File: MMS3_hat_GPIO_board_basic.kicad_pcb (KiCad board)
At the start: 4 copper layers, 100 x 50 mm, 55 parts, among them J1 Chainbus in, J2 Chainbus Out, J3 Conn_01x04_Pin, J4 AMASS XT60 Male, J5 AMASS XT60 Female, J8 Conn_01x03_Pin, SW1 SW_DIP_x04, U1 SN74CB3Q3384APW, U2 M24C64, U4 AMS1117, U5 LM2596HVS-ADJRG

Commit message: added routing and gerber
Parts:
- removed C16, C18: 10uF, PCM_JLCPCB:C_0603
- removed C17, C19, C25, C26, C27, C28: 47u, Capacitor_SMD:CP_Elec_6.3x7.7
- removed C20, C21, C23, C24: 100nF, PCM_JLCPCB:C_0603
- removed C22: 3.3nF, PCM_JLCPCB:C_0603
- removed D2, D4: MBRD10100CTTR, SMC_MBRD10100CTTR:TO-252-3_L6.5-W5.8-P4.58-TL
- removed J4: AMASS XT60 Male, XT60:AMASS_XT60PW-M_1x02_P7.20mm_Horizontal
- removed L1: 100uH 4A, Inductor_SMD:L_Sunlord_SWRB1207S
- removed R10, R11, R17, R18: 33kΩ, PCM_JLCPCB:R_0402
- removed R12: 1kΩ, PCM_JLCPCB:R_0402
- removed R13: 18.7k, PCM_JLCPCB:R_0402
- removed R14: 16.5k, PCM_JLCPCB:R_0402
- removed R15: 9.53k, PCM_JLCPCB:R_0402
- removed R16: 5.11k, PCM_JLCPCB:R_0402
- removed SW1: SW_DIP_x04, Button_Switch_THT:SW_DIP_SPSTx04_Slide_6.7x11.72mm_W7.62mm_P2.54mm_LowProfile
- removed TP8: TestPoint, TestPoint:TestPoint_Pad_D1.0mm
- removed U5: LM2596HVS-ADJRG, Package_TO_SOT_SMD:TO-263-5_TabPin3
- added C3: 10uF, PCM_JLCPCB:C_0603, F.Cu at (107.8, 106.0)
- added C4: 10uF, PCM_JLCPCB:C_0603, F.Cu at (110.3, 110.9)
- added C5: 10uF, PCM_JLCPCB:C_0603, F.Cu at (108.6, 110.9)
- added C6: 100n, PCM_JLCPCB:C_0603, F.Cu at (131.0, 111.5)
- added J10: Conn_01x03_Pin, Connector_JST:JST_XH_S3B-XH-A_1x03_P2.50mm_Horizontal, F.Cu at (125.7, 133.6)
- added J11: Conn_01x03_Pin, Connector_JST:JST_XH_S3B-XH-A_1x03_P2.50mm_Horizontal, F.Cu at (137.7, 133.6)
- added J12: Conn_01x03_Pin, Connector_JST:JST_XH_S3B-XH-A_1x03_P2.50mm_Horizontal, F.Cu at (149.6, 133.6)
- added J13: Conn_01x03_Pin, Connector_JST:JST_XH_S3B-XH-A_1x03_P2.50mm_Horizontal, F.Cu at (161.6, 133.6)
- added J14: Conn_01x03_Pin, Connector_JST:JST_XH_S3B-XH-A_1x03_P2.50mm_Horizontal, F.Cu at (174.6, 127.4)
- added J15: Conn_01x03_Pin, Connector_JST:JST_XH_S3B-XH-A_1x03_P2.50mm_Horizontal, F.Cu at (174.6, 115.5)
- added J16: Conn_01x03_Pin, Connector_JST:JST_XH_S3B-XH-A_1x03_P2.50mm_Horizontal, F.Cu at (174.6, 103.5)
- added J6: Conn_01x03_Pin, Connector_JST:JST_XH_S3B-XH-A_1x03_P2.50mm_Horizontal, F.Cu at (82.4, 122.4)
- added J7: Conn_01x03_Pin, Connector_JST:JST_XH_S3B-XH-A_1x03_P2.50mm_Horizontal, F.Cu at (89.5, 133.6)
- added J9: Conn_01x03_Pin, Connector_JST:JST_XH_S3B-XH-A_1x03_P2.50mm_Horizontal, F.Cu at (113.8, 133.6)
- added PIN 1: Conn_01x03_Pin, Connector_JST:JST_XH_S3B-XH-A_1x03_P2.50mm_Horizontal, F.Cu at (82.4, 98.5)
- added U3: AMS1117, PCM_JLCPCB:SOT-223-3_L6.5-W3.4-P2.30-LS7.0-BR, F.Cu at (103.0, 110.0)
- J5: value AMASS XT60 Female -> Conn_01x03_Pin; footprint XT60:AMASS_XT60PW-F_1x02_P7.20mm_Horizontal -> Connector_JST:JST_XH_S3B-XH-A_1x03_P2.50mm_Horizontal
- J8: footprint Connector_PinHeader_2.54mm:PinHeader_1x03_P2.54mm_Vertical -> Connector_JST:JST_XH_S3B-XH-A_1x03_P2.50mm_Horizontal
- U4: value AMS1117 -> TCA9535PWR; footprint PCM_JLCPCB:SOT-223-3_L6.5-W3.4-P2.30-LS7.0-BR -> Package_SO:TSSOP-24_4.4x7.8mm_P0.65mm
- moved U4 41.4 mm to (127.7, 117.2)
- moved J8 10.9 mm to (101.5, 133.6), turned to 0 degrees
- moved J5 10.2 mm to (82.4, 110.5), turned to -90 degrees
- moved D1 9.75 mm to (168.0, 95.0)
- moved R1 9.75 mm to (166.2, 94.7)
- moved R2 0.94 mm to (157.5, 96.9)
- moved R3 0.89 mm to (158.6, 96.9)
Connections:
- J5 pad 2: Vin -> /GPIO_Expander/P01
- J8 pad 1: Net-(J8-Pin_1) -> GND
- J8 pad 2: Vin -> /GPIO_Expander/P04
- J8 pad 3: U_reg -> +3V3
- U4 pad 1: GND -> unconnected-(U4-~{INT}-Pad1)
- U4 pad 2: +3V3 -> GND
- U4 pad 3: +5V -> GND
- U4 pad 4: +3V3 -> /GPIO_Expander/P00
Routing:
- net +3V3: track 46.9 -> 291.5 mm, vias 1 -> 4
- net Vin: track 64.3 -> 0.00 mm
- net U_reg: track 55.0 -> 0.00 mm, vias 2 -> 0
- net /GPIO_Expander/P14: track 0.00 -> 51.4 mm
- net /GPIO_Expander/P00: track 0.00 -> 48.4 mm, vias 0 -> 1
- net /GPIO_Expander/P13: track 0.00 -> 46.4 mm
- net /GPIO_Expander/P12: track 0.00 -> 46.2 mm
- net /GPIO_Expander/P02: track 0.00 -> 45.7 mm
- net /GPIO_Expander/P01: track 0.00 -> 43.7 mm
- net /GPIO_Expander/P03: track 0.00 -> 39.4 mm
- net /GPIO_Expander/P11: track 0.00 -> 39.1 mm
- net Net-(U5-FB): track 38.3 -> 0.00 mm, vias 1 -> 0
- net +5V: track 59.4 -> 25.8 mm, vias 5 -> 3
- net /GPIO_Expander/P04: track 0.00 -> 27.2 mm
- net BRD_VIN: track 27.1 -> 0.00 mm
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- removed copper zone on In1.Cu, net GND
- removed copper zone on In2.Cu, net GND
- removed copper zone on F.Cu, net Net-(C20-Pad2)
- removed copper zone on F.Cu, net Net-(C23-Pad2)
- removed copper zone on F.Cu, net Net-(D4-K)
- removed copper zone on F.Cu, net Net-(J8-Pin_1)
- removed copper zone on F.Cu, net U_reg
- removed copper zone on B.Cu, net Vin
- removed copper zone on F.Cu, net Vin
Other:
- copper layers 4 -> 2
- board text added: "PIN 1"
- board text added: "PIN 10"
- board text added: "PIN 11"
- board text added: "PIN 12"
- board text added: "PIN 13"
- board text added: "PIN 2"
- board text added: "PIN 3"
- board text added: "PIN 4"
- board text added: "PIN 5"
- board text added: "PIN 6"
- board text added: "PIN 7"
- board text added: "PIN 8"
- board text added: "PIN 9"
- board text removed: "DONT change SW1 WITH POWER ON"
- board text removed: "SW1 24 9 12 6.2"

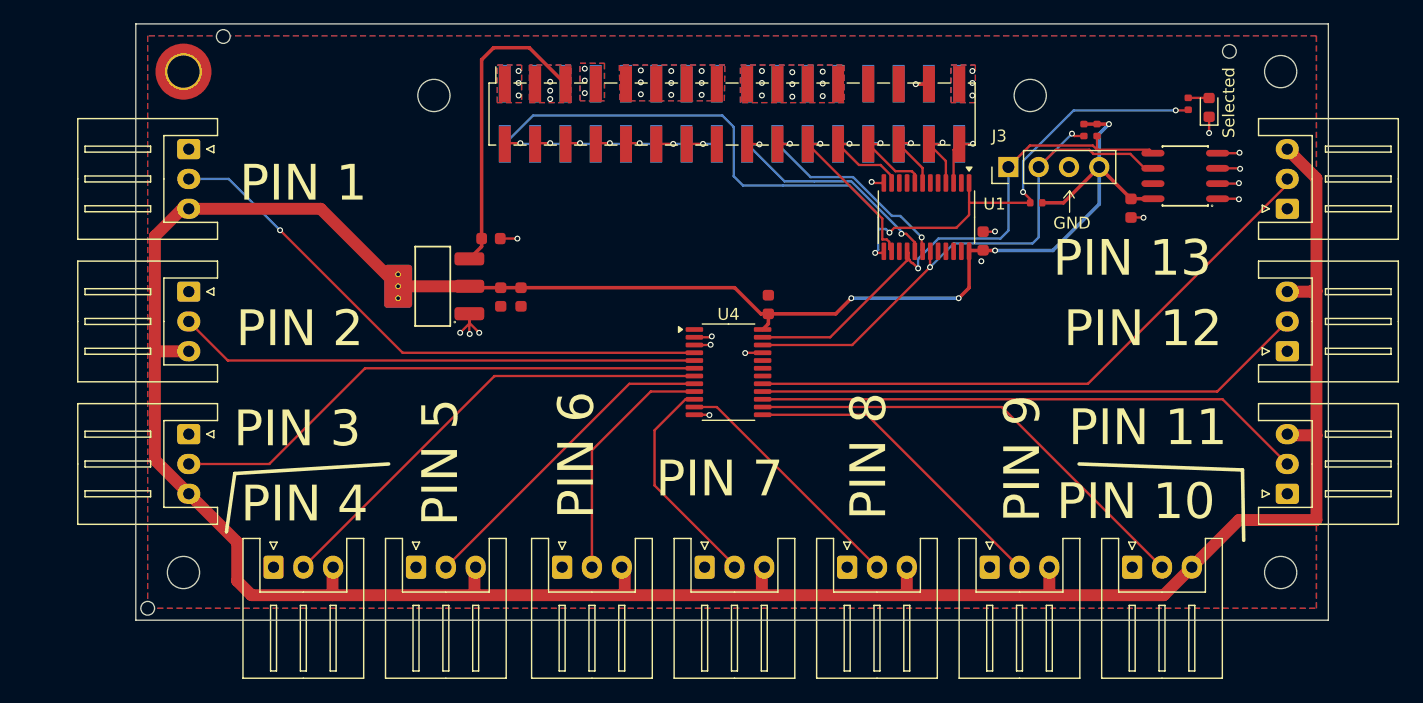
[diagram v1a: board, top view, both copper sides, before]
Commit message: added adc
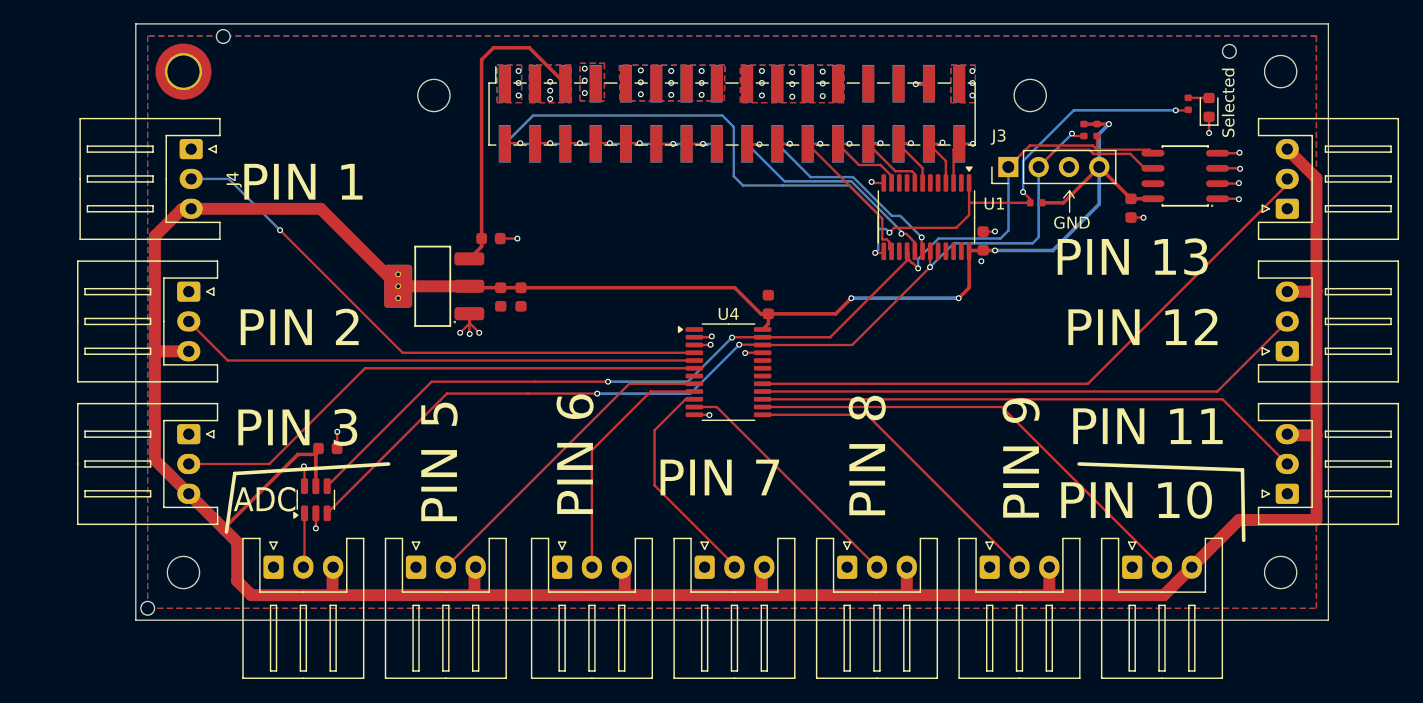
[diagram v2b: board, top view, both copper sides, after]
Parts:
- removed PIN 1: Conn_01x03_Pin, Connector_JST:JST_XH_S3B-XH-A_1x03_P2.50mm_Horizontal
- added C7: 100n, PCM_JLCPCB:C_0603, F.Cu at (94.1, 123.6)
- added J4: Conn_01x03_Pin, Connector_JST:JST_XH_S3B-XH-A_1x03_P2.50mm_Horizontal, F.Cu at (82.6, 98.5)
- added U5: MCP3421A0T-ECH, Package_TO_SOT_SMD:SOT-23-6, F.Cu at (93.1, 127.9)
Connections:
- J7 pad 2: /GPIO_Expander/P03 -> /GPIO_Expander/ADC
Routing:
- net /Bus_switch/Chainbus.SCL: track 50.0 -> 92.4 mm, vias 2 -> 4
- net /Bus_switch/Chainbus.SDA: track 46.4 -> 88.1 mm, vias 1 -> 3
- net /GPIO_Expander/P03: track 39.4 -> 0.00 mm
- net +3V3: track 291.5 -> 305.0 mm
- net /GPIO_Expander/ADC: track 0.00 -> 4.56 mm
- net GND: track 24.7 -> 29.1 mm, vias 35 -> 38
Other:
- board text added: "ADC"
- board text removed: "PIN 4"

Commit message: cosmetic changes
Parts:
- removed the G*** at (106.2, 117.5)
- added G***: LOGO, Shitposting:Rick_roll_10mm, B.Cu at (105.8, 119.0)
- added G***: LOGO, Shitposting:Basic_Megamind_15mm, B.Cu at (161.1, 120.2)
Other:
- board text added: "3"
- board text added: "DEVICE SENSETIVE DONT SCREAM"
- board text added: "Yada Yada EU not qualified Dont use in final prducts frfr"
- board text removed: "2"
- board text removed: "DEVICE ESD SENSETIVE"
- board text removed: "This is prototype device It is not certified according to current EU laws. Do not sell or use outside of research purposes."

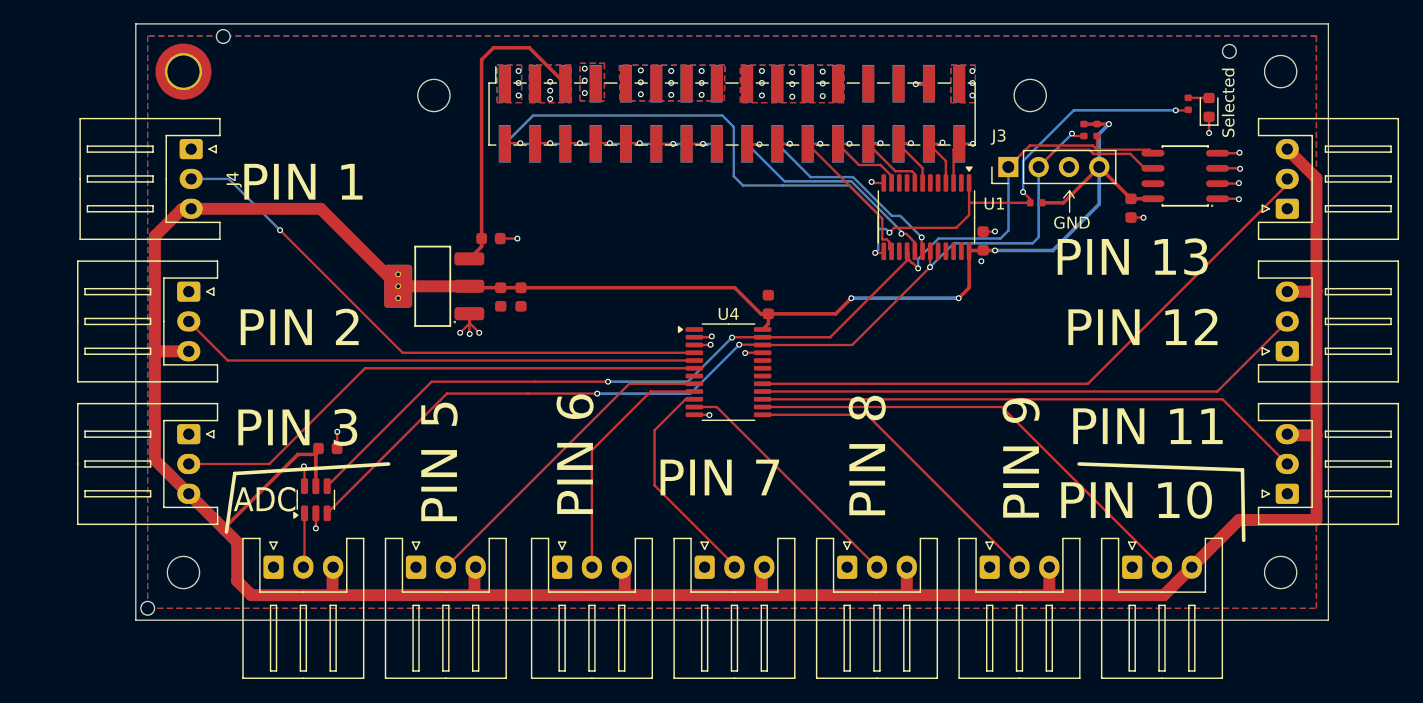
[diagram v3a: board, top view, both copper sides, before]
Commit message: added leds and bom. Revison 1.2
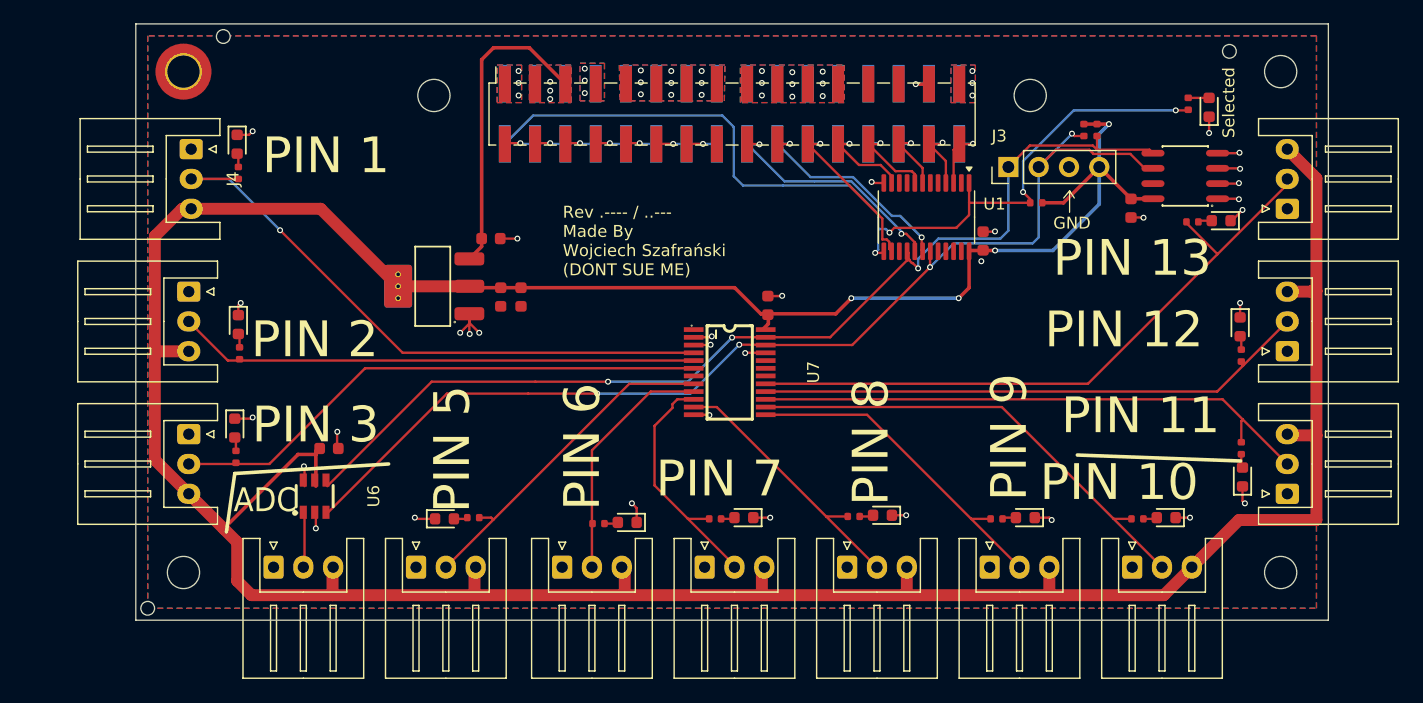
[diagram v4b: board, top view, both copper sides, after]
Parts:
- removed D1: LED, LED_SMD:LED_0603_1608Metric
- removed U4: TCA9535PWR, Package_SO:TSSOP-24_4.4x7.8mm_P0.65mm
- removed U5: MCP3421A0T-ECH, Package_TO_SOT_SMD:SOT-23-6
- added D10: Red, PCM_JLCPCB:D_0603, F.Cu at (170.8, 126.0)
- added D11: Red, PCM_JLCPCB:D_0603, F.Cu at (119.2, 129.8)
- added D12: Red, PCM_JLCPCB:D_0603, F.Cu at (103.9, 129.5)
- added D13: Red, PCM_JLCPCB:D_0603, F.Cu at (86.3, 121.9)
- added D14: Red, PCM_JLCPCB:D_0603, F.Cu at (86.6, 113.2)
- added D15: Red, PCM_JLCPCB:D_0603, F.Cu at (86.5, 98.1)
- added D2: Red, PCM_JLCPCB:D_0603, F.Cu at (168.0, 95.0)
- added D3: Red, PCM_JLCPCB:D_0603, F.Cu at (129.0, 129.4)
- added D4: Red, PCM_JLCPCB:D_0603, F.Cu at (140.6, 129.2)
- added D5: Red, PCM_JLCPCB:D_0603, F.Cu at (164.4, 129.4)
- added D6: Red, PCM_JLCPCB:D_0603, F.Cu at (152.6, 129.4)
- added D8: Red, PCM_JLCPCB:D_0603, F.Cu at (169.0, 104.5)
- added D9: Red, PCM_JLCPCB:D_0603, F.Cu at (170.6, 113.4)
- added R10: 330Ω, PCM_JLCPCB:R_0402, F.Cu at (166.6, 104.6)
- added R11: 330Ω, PCM_JLCPCB:R_0402, F.Cu at (170.7, 115.8)
- added R12: 330Ω, PCM_JLCPCB:R_0402, F.Cu at (170.7, 123.6)
- added R13: 330Ω, PCM_JLCPCB:R_0402, F.Cu at (116.8, 129.9)
- added R14: 330Ω, PCM_JLCPCB:R_0402, F.Cu at (106.3, 129.4)
- added R15: 330Ω, PCM_JLCPCB:R_0402, F.Cu at (86.4, 124.3)
- added R16: 330Ω, PCM_JLCPCB:R_0402, F.Cu at (86.7, 115.6)
- added R17: 330Ω, PCM_JLCPCB:R_0402, F.Cu at (86.6, 100.5)
- added R5: 330Ω, PCM_JLCPCB:R_0402, F.Cu at (126.6, 129.5)
- added R6: 330Ω, PCM_JLCPCB:R_0402, F.Cu at (138.2, 129.3)
- added R7: 330Ω, PCM_JLCPCB:R_0402, F.Cu at (162.0, 129.5)
- added R8: 330Ω, PCM_JLCPCB:R_0402, F.Cu at (150.2, 129.5)
- added U6: MCP3421A0T-E/CH, MCP3421A0T:SOT-23-6_L2.9-W1.6-P0.95-LS2.8-BR, F.Cu at (93.0, 127.6)
- added U7: TCA9535PWR_C130204, TCA9535PWR:TSSOP-24_L7.8-W4.4-P0.65-LS6.4-BL, F.Cu at (127.8, 117.2)
- C6, C7: value 100n -> 100nF
- moved C7 0.10 mm to (94.2, 123.6)
- moved C6 0.08 mm to (131.0, 111.6)
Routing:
- net GND: track 29.1 -> 47.6 mm, vias 38 -> 51
- net /GPIO_Expander/P00: track 48.4 -> 52.4 mm
- net /GPIO_Expander/P14: track 51.4 -> 55.2 mm
- net /GPIO_Expander/P06: track 18.7 -> 20.9 mm
- net /GPIO_Expander/P12: track 46.2 -> 48.2 mm
- net /GPIO_Expander/P07: track 20.9 -> 22.7 mm
- net /GPIO_Expander/P10: track 26.8 -> 28.5 mm
- net /GPIO_Expander/P11: track 39.1 -> 40.5 mm
- net /GPIO_Expander/P04: track 27.2 -> 28.5 mm
- net Net-(D4-Pad2): track 0.00 -> 1.16 mm
- net Net-(D10-Pad2): track 0.00 -> 1.16 mm
- net Net-(D14-Pad2): track 0.00 -> 1.16 mm
- net Net-(D8-Pad2): track 0.00 -> 1.16 mm
- net Net-(D6-Pad2): track 0.00 -> 1.16 mm
- net Net-(D9-Pad2): track 0.00 -> 1.16 mm
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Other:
- board text added: "Rev .---- / ..--- Made By Wojciech Szafrański (DONT SUE ME)"

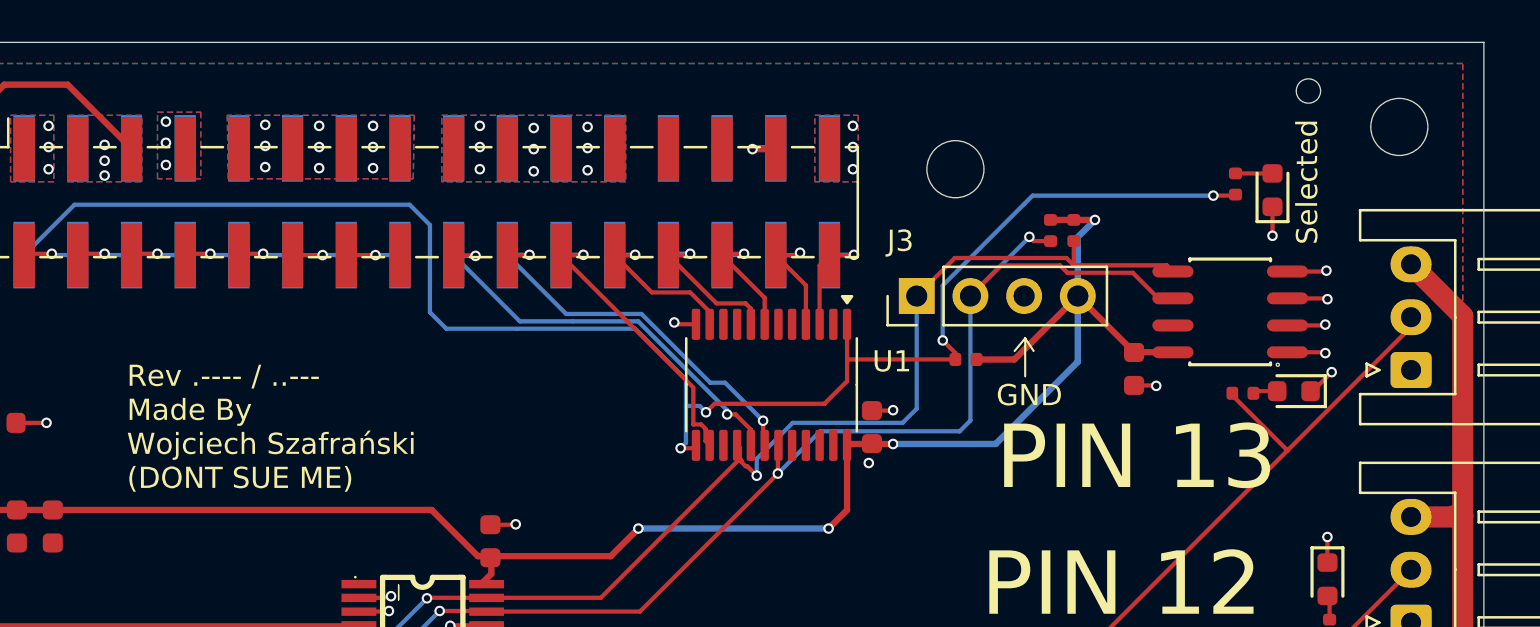
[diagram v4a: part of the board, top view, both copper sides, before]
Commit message: fixed selected led polarity
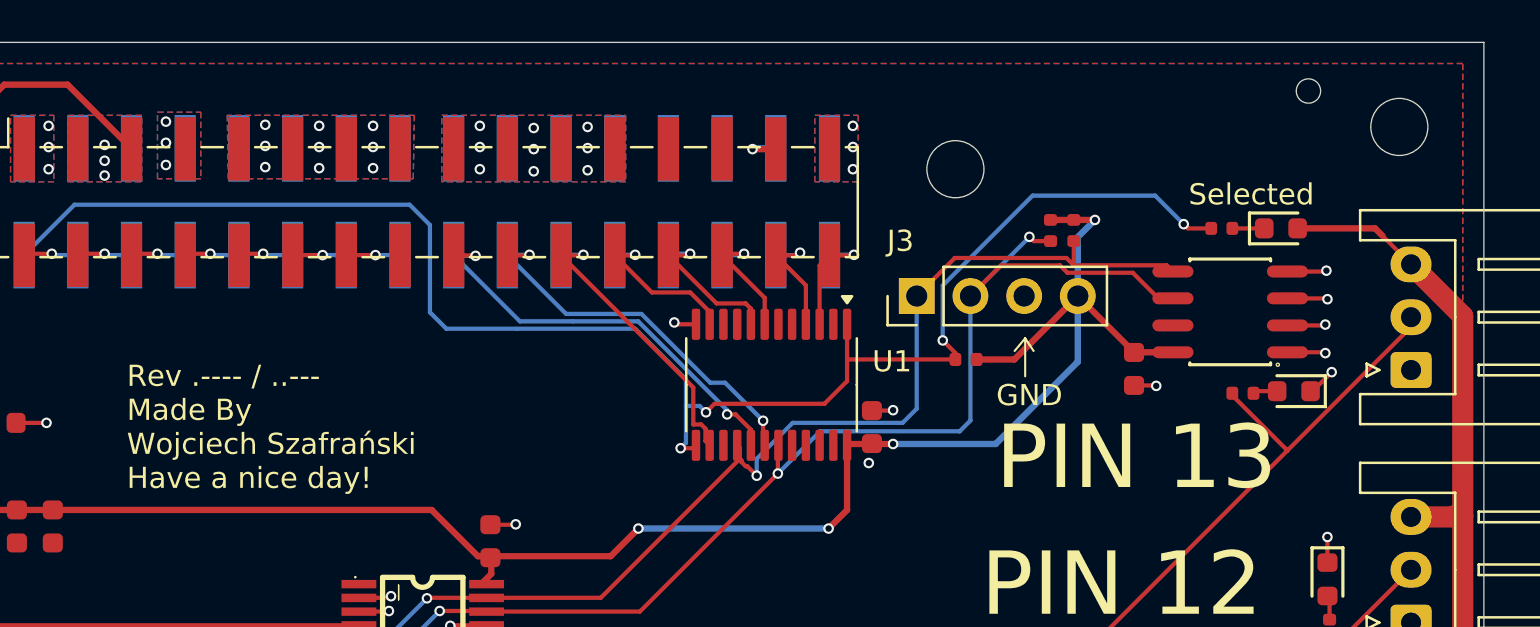
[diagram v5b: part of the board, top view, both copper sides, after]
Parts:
- removed PN1: ~, PCM_JLCPCB:Part_Num_JLCPCB
- moved R1 2.20 mm to (165.6, 96.8), turned to 0 degrees
- moved D2 1.85 mm to (168.4, 96.8), turned to 0 degrees
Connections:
- D2 pad 1: GND -> Net-(D2-Pad1)
- D2 pad 2: Net-(D2-Pad2) -> +3V3
- R1 pad 2: Net-(D2-Pad2) -> Net-(D2-Pad1)
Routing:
- net +3V3: track 305.0 -> 311.1 mm
- net GND: track 47.6 -> 46.0 mm, vias 51 -> 50
- net Net-(D2-Pad2): track 1.52 -> 0.00 mm
- net Net-(D2-Pad1): track 0.00 -> 1.51 mm
- net /Bus_switch/SEL1: track 77.8 -> 77.3 mm
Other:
- board text added: "Rev .---- / ..--- Made By Wojciech Szafrański Have a nice day!"
- board text removed: "Rev .---- / ..--- Made By Wojciech Szafrański (DONT SUE ME)"
